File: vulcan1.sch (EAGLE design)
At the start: 0 parts

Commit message: update
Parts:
- added C1, C2, C3: .1u, adafruit:C-US025-040X050
- added C4: 4.7u, adafruit:CPOL-USE5-8.5
- added C5: 10n, adafruit:C-US025-040X050
- added U$1: STM32F103XX-48PIN, vulcan-1:STM32F103XX-48PIN
- added U$2: A2200-A, vulcan-1:A2200-A
- added U$3, U$4: TPS63060, vulcan-1:TPS63060
- added U$5, U$6: ASPI-0520LR, vulcan-1:ASPI-0520LR
- added U$7: AD8494ARMZ, vulcan-1:AD8494ARMZ
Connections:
- new net GND: C4.-, C5.2, U$1.VDDA, U$1.VSS_1, U$1.VSS_2, U$1.VSS_3
- new net N$1: C4.+, U$1.VDD_1, U$1.VDD_2, U$1.VDD_3
- new net N$2: C5.1, U$1.VSSA
- new net N$3: U$4.L1, U$5.P$1
- new net N$4: U$4.L2, U$5.P$2
- new net N$5: U$3.L1, U$6.P$1
- new net N$6: U$3.L2, U$6.P$2

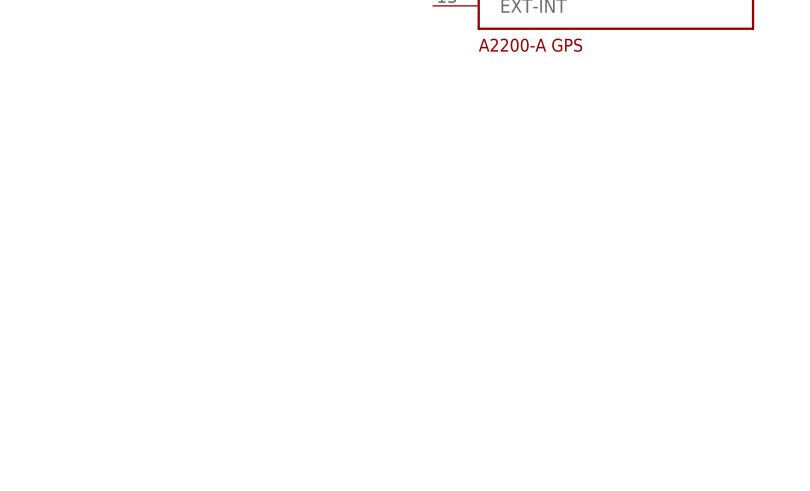
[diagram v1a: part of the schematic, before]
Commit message: update
crystal and RTC
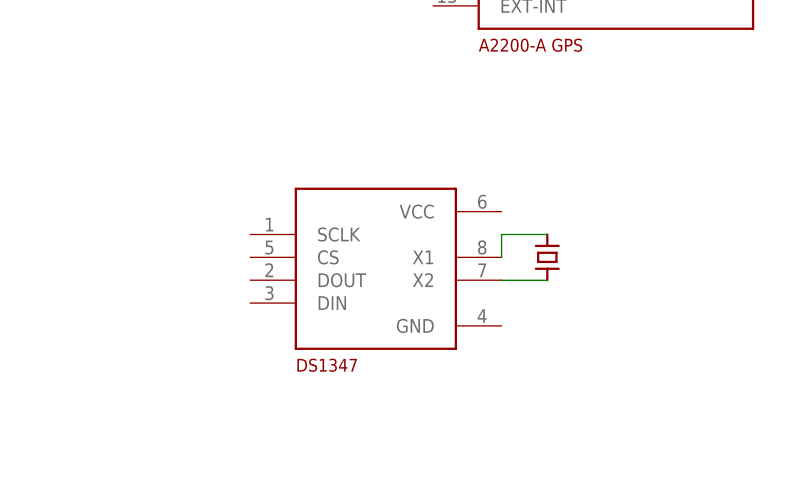
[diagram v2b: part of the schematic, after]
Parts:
- added U$8: 32.768khz, vulcan-1:ECX-306X
- added U$9: DS1347, vulcan-1:DS1347
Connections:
- new net N$7: U$8.P$1, U$9.X2
- new net N$8: U$8.P$2, U$9.X1
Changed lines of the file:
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@@
 <part name="U$6" library="vulcan-1" deviceset="ASPI-0520LR" device=""/>
 <part name="U$7" library="vulcan-1" deviceset="AD8494ARMZ" device=""/>
+<part name="U$8" library="vulcan-1" deviceset="ECX-306X" device="" value="32.768khz"/>
+<part name="U$9" library="vulcan-1" deviceset="DS1347" device=""/>
 </parts>
 <sheets>
@@
 <instance part="U$6" gate="G$1" x="-127" y="109.22"/>
 <instance part="U$7" gate="G$1" x="-7.62" y="101.6"/>
+<instance part="U$8" gate="G$1" x="124.46" y="-25.4" rot="R90"/>
+<instance part="U$9" gate="G$1" x="104.14" y="-30.48"/>
 </instances>
 <busses>
@@
 </segment>
 </net>
+<net name="N$7" class="0">
+<segment>
+<pinref part="U$8" gate="G$1" pin="P$1"/>
+<pinref part="U$9" gate="G$1" pin="X2"/>
+<wire x1="124.46" y1="-27.94" x2="119.38" y2="-27.94" width="0.1524" layer="91"/>
+</segment>
+</net>
+<net name="N$8" class="0">
+<segment>
+<pinref part="U$8" gate="G$1" pin="P$2"/>
+<wire x1="124.46" y1="-22.86" x2="119.38" y2="-22.86" width="0.1524" layer="91"/>
+<pinref part="U$9" gate="G$1" pin="X1"/>
+<wire x1="119.38" y1="-22.86" x2="119.38" y2="-25.4" width="0.1524" layer="91"/>
+</segment>
+</net>

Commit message: update
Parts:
- added BKP-BATT: (no value), adafruit:CR1220THM
- added C10, C9: 18pf, adafruit:C-US025_050-045X075
- added C11, C12, C16, C17, C18, C6, C7: .1u, adafruit:C-US025_050-045X075
- added C13, C8: 10pf, adafruit:C-US025_050-045X075
- added C14, C15: 4700uf, adafruit:CPOL-USE5-13
- added C19: 1u, adafruit:C-US025_050-045X075
- added D1, D2: (no value), adafruit:SCHOTTKY-DIODEDO35-7
- added JP1: M025MM, SparkFun-Connectors:M025MM
- added R1, R3: 560k, adafruit:R-US_0204/7
- added R2, R4: 100k, adafruit:R-US_0204/7
- added R5: 10k, adafruit:R-US_0204/7
- added U$10: HC/49US(AT49), vulcan-1:HC/49US(AT49)
- added U$11: BMP183, vulcan-1:BMP183
- added U$12: XBEE, adafruit:XBEE
- added U1: SD_CARD_SOCKET4UCON, SparkFun-Connectors:SD_CARD_SOCKET4UCON
- C1, C2, C3, C5: device adafruit:C-US025-040X050 -> adafruit:C-US025_050-045X075
- U$8: value 32.768khz -> DS1347; device vulcan-1:ECX-306X -> vulcan-1:DS1347
- U$9: value DS1347 -> ECX-306X; device vulcan-1:DS1347 -> vulcan-1:ECX-306X
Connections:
- new net 3.3A: R1.2, U$3.VOUT
- new net 3.3B: R3.2, U$4.VOUT
- new net CLK: U1.CLK
- new net GPS-DIN: U$2.RX0
- new net GPS-DOUT: U$2.TX0
- new net MISO: U1.DAT0
- new net MOSI: U1.CMD
- new net N$10: C9.1, U$1.PD0_OSC_IN, U$10.P$2
- new net N$11: C7.1, U$3.VAUX
- new net N$12: C18.1, C19.1, D1.C, D2.C, U$8.VCC
- new net N$13: U$11.VDD
- new net N$14: C8.1, R1.1, R2.2, U$3.FB
- new net N$15: C13.1, R3.1, R4.2, U$4.FB
- new net N$16: C16.1, U$2.VCC
- new net N$17: U$2.ANT_GND
- new net N$18: C12.1, U$4.VAUX
- new net N$19: U$2.ANT_IN
- new net N$20: R5.2, U$2.VOUT
- new net N$21: R5.1, U$2.GPIO6
- new net N$22: U$11.VDDIO
- new net N$25: U1.VDD
- new net N$26: D2.A
- new net N$9: C10.1, U$1.PD1_OSC_OUT, U$10.P$1
- new net SD-CS: U1.CD/DAT3
- new net V-BKP: BKP-BATT.+, D1.A
- new net VB-EN: U$4.EN
- new net VBAT: C11.1, C14.+, C15.+, C6.1, JP1.2, U$3.EN, U$3.VIN, U$4.VIN
- new net VCC: C17.1, U$12.VCC
- new net XBEE-CS: U$12.CTS/DIO7
- new net XBEE-DIN: U$12.DIN
- new net XBEE-DOUT: U$12.DOUT
- new net XBEE-RTS: U$12.RTS/AD6/DIO6
- net GND: now also BKP-BATT.-, C1.2, C10.2, C11.2, C12.2, C13.2, C15.-, C16.2, C17.2, C18.2, C19.2, C2.2, C3.2, C6.2, C7.2, C8.2, C9.2, JP1.1, R2.1, R4.1, U$11.GND, U$12.GND, U$2.GND_1, U$2.GND_2, U$3.GND, U$3.PG, U$3.PGND, U$3.PS/SYNC, U$4.GND, U$4.PG, U$4.PGND, U$4.PS/SYNC, U$7.V-, U$8.GND
- net N$1: now also C1.1, C2.1, C3.1
- net N$7: now also U$8.X2, U$9.P$1; no longer U$8.P$1, U$9.X2
- net N$8: now also U$8.X1, U$9.P$2; no longer U$8.P$2, U$9.X1
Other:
- note added: "3.3V supply A"
- note added: "3.3V supply B"
- note added: "7.4V Li-Po and capcitor bank"
- note added: "Backup battery"
- note added: "GPS module"
- note added: "MICROCONTROLLER"
- note added: "PERIPHERALS"
- note added: "POWER"
- note added: "Pressure sensor"
- note added: "Real Time Clock"
- note added: "SD Card"
- note added: "Thermocouple amp"
- note added: "XBEE Radio Module"
- moved on the sheet: C1, C2, C3, C4, C5

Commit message: update
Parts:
- added C20, C21, C22: .1u, adafruit:C-US025-030X050
- added U$13: 2X24HEADER, vulcan-1:2X24HEADER
- C1, C10, C11, C12, C13, C16, C17, C18, C2, C3, C5, C6, C7, C8, C9: device adafruit:C-US025_050-045X075 -> adafruit:C-US025-030X050
- C19: device adafruit:C-US025_050-045X075 -> adafruit:CPOL-USE2,5-6E
- C4: device adafruit:CPOL-USE5-8.5 -> adafruit:CPOL-USE2,5-6E
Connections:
- net N$19 renamed GPS-ANT
- net XBEE-DIN renamed USART3-TX
- removed net CLK: U1.CLK
- removed net GPS-DIN: U$2.RX0
- removed net GPS-DOUT: U$2.TX0
- removed net MISO: U1.DAT0
- removed net MOSI: U1.CMD
- removed net N$1: C1.1, C2.1, C3.1, C4.+, U$1.VDD_1, U$1.VDD_2, U$1.VDD_3
- removed net N$13: U$11.VDD
- removed net N$16: C16.1, U$2.VCC
- removed net N$17: U$2.ANT_GND
- removed net N$22: U$11.VDDIO
- removed net N$25: U1.VDD
- removed net N$26: D2.A
- removed net VCC: C17.1, U$12.VCC
- removed net XBEE-CS: U$12.CTS/DIO7
- removed net XBEE-DOUT: U$12.DOUT
- removed net XBEE-RTS: U$12.RTS/AD6/DIO6
- new net ACC-CS: U$13.P$6
- new net ACC-FLAG: U$13.P$7
- new net ACC-RST: U$13.P$8
- new net BOOT0: U$1.BOOT0
- new net BOOT1: U$1.PB2
- new net N$23: U$2.ON_OFF
- new net N$24: U$7.+IN, U$7.-IN
- new net N$30: U$7.OUT, U$7.SENSE
- new net PS-CS: U$11.CSB
- new net RTC-CS: U$8.CS
- new net SPI-MISO: U$1.PA6, U$11.SDO, U$13.P$4, U$8.DOUT, U1.DAT0
- new net SPI-MOSI: U$1.PA7, U$11.SDI, U$13.P$5, U$8.DIN, U1.CMD
- new net SPI-NSS: U$1.PA4
- new net SPI-SCK: U$1.PA5, U$11.SCK, U$13.P$3, U$8.SCLK, U1.CLK
- new net USART1-RX: U$1.PA10
- new net USART1-TX: U$1.PA9
- new net USART2-RX: U$1.PA3, U$2.TX0
- new net USART2-TX: U$1.PA2, U$1.PB10, U$2.RX0
- new net USART3-CTS: U$1.PB13, U$12.CTS/DIO7
- new net USART3-RTS: U$1.PB14, U$12.RTS/AD6/DIO6
- new net USART3-RX: U$1.PB11, U$12.DOUT
- net 3.3A: now also C1.1, C2.1, C20.1, C21.1, C22.1, C3.1, C4.+, D2.A, U$1.VDD_1, U$1.VDD_2, U$1.VDD_3, U$11.VDD, U$11.VDDIO, U$13.P$10, U$13.P$11, U$13.P$12, U$7.V+, U1.VDD
- net 3.3B: now also C16.1, C17.1, U$12.VCC, U$2.VCC
- net GND: now also C19.-, C20.2, C21.2, C22.2, U$13.P$13, U$13.P$14, U$13.P$15, U$2.ANT_GND, U$7.REF, U1.VSS1, U1.VSS2; no longer C19.2
- net N$12: now also C19.+; no longer C19.1
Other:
- note added: "Accelerometer mount"

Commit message: update-all but RF traces and gnd plane done
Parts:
- removed U$13: 2X24HEADER, vulcan-1:2X24HEADER
- added A2200-A: A2200-A, vulcan-1:A2200-A
- added FUSE: FUSE, adafruit:R-US_0204/7
- added JP2: (no value), adafruit:PINHD-1X8CLEANBIG
- added JP3: (no value), adafruit:PINHD-1X3CB
- added Q1, Q2: IRF540, transistor-power:IRF540
- added R6, R7: 10k, adafruit:R-US_0204/7
- added T1, T2: 2N3904, transistor:2N3904
- added TPS63060-A, TPS63060-B: TPS63060, vulcan-1:TPS63060
- C14: value 4700uf -> .1u; device adafruit:CPOL-USE5-13 -> adafruit:C-US025-030X050
- U$2: value A2200-A -> 2X3; device vulcan-1:A2200-A -> vulcan-1:2X3
- U$3, U$4: value TPS63060 -> 1X2BIG; device vulcan-1:TPS63060 -> vulcan-1:1X2BIG
- U$7: value AD8494ARMZ -> SMA; device vulcan-1:AD8494ARMZ -> vulcan-1:SMA
- renumbered U$11 to BMP183, U$12 to XBEE, U$8 to DS1347, U1 to SD
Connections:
- removed net N$23: U$2.ON_OFF
- removed net N$24: U$7.+IN, U$7.-IN
- removed net N$30: U$7.OUT, U$7.SENSE
- removed net SPI-NSS: U$1.PA4
- removed net VB-EN: U$4.EN
- new net EMATCH1: T1.B
- new net EMATCH2: T2.B
- new net GPS-CS: A2200-A.ON_OFF, U$1.PA1
- new net N$1: Q1.G, R6.1, T1.C
- new net N$13: Q1.D, U$3.2
- new net N$16: Q2.G, R7.1, T2.C
- new net N$17: Q2.D, U$4.2
- new net VB-CS: TPS63060-B.EN, U$1.PB8
- new net VBAT-F: FUSE.2, R6.2, R7.2, U$3.1, U$4.1
- net 3.3A: now also C14.1, JP2.8, TPS63060-A.VOUT, U$2.1, U$2.2; no longer C22.1, U$13.P$10, U$13.P$11, U$13.P$12, U$3.VOUT, U$7.V+
- net 3.3B: now also A2200-A.VCC, C22.1, TPS63060-B.VOUT; no longer U$2.VCC, U$4.VOUT
- net ACC-CS: now also JP2.5, U$1.PA8; no longer U$13.P$6
- net ACC-FLAG: now also JP2.6; no longer U$13.P$7
- net ACC-RST: now also JP2.4; no longer U$13.P$8
- net BOOT0: now also U$2.3
- net BOOT1: now also U$2.4
- net GND: now also A2200-A.ANT_GND, A2200-A.GND_1, A2200-A.GND_2, C14.2, JP2.7, JP3.3, Q1.S, Q2.S, T1.E, T2.E, TPS63060-A.GND, TPS63060-A.PG, TPS63060-A.PGND, TPS63060-A.PS/SYNC, TPS63060-B.GND, TPS63060-B.PG, TPS63060-B.PGND, TPS63060-B.PS/SYNC, U$2.5, U$2.6; no longer U$13.P$13, U$13.P$14, U$13.P$15, U$2.ANT_GND, U$2.GND_1, U$2.GND_2, U$3.GND, U$3.PG, U$3.PGND, U$3.PS/SYNC, U$4.GND, U$4.PG, U$4.PGND, U$4.PS/SYNC, U$7.REF, U$7.V-
- net GPS-ANT: now also A2200-A.ANT_IN, U$7.IN; no longer U$2.ANT_IN
- net N$11: now also TPS63060-A.VAUX; no longer U$3.VAUX
- net N$14: now also TPS63060-A.FB; no longer U$3.FB
- net N$15: now also TPS63060-B.FB; no longer U$4.FB
- net N$18: now also TPS63060-B.VAUX; no longer U$4.VAUX
- net N$20: now also A2200-A.VOUT; no longer U$2.VOUT
- net N$21: now also A2200-A.GPIO6; no longer U$2.GPIO6
- net N$3: now also TPS63060-B.L1; no longer U$4.L1
- net N$4: now also TPS63060-B.L2; no longer U$4.L2
- net N$5: now also TPS63060-A.L1; no longer U$3.L1
- net N$6: now also TPS63060-A.L2; no longer U$3.L2
- net PS-CS: now also U$1.PA4
- net RTC-CS: now also U$1.PB12
- net SD-CS: now also U$1.PB15
- net SPI-MISO: now also JP2.2; no longer U$13.P$4
- net SPI-MOSI: now also JP2.1; no longer U$13.P$5
- net SPI-SCK: now also JP2.3; no longer U$13.P$3
- net USART1-RX: now also JP3.2
- net USART1-TX: now also JP3.1
- net USART2-RX: now also A2200-A.TX0; no longer U$2.TX0
- net USART2-TX: now also A2200-A.RX0; no longer U$1.PB10, U$2.RX0
- net USART3-TX: now also U$1.PB10
- net VBAT: now also FUSE.1, TPS63060-A.EN, TPS63060-A.VIN, TPS63060-B.VIN; no longer C14.+, U$3.EN, U$3.VIN, U$4.VIN
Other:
- note added: "Accelerometer Header"
- note added: "BOOT header"
- note added: "E-Matches"
- note removed: "Accelerometer mount"
- note removed: "Thermocouple amp"
- moved on the sheet: C1, C10, C2, C20, C22, C3, C4, C5, C9

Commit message: update-gnd done
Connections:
- net GND: now also U$7.OUT
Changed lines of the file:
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@@
 <pinref part="GND17" gate="1" pin="GND"/>
 <wire x1="139.7" y1="7.62" x2="149.86" y2="7.62" width="0.1524" layer="91"/>
-<wire x1="149.86" y1="7.62" x2="149.86" y2="2.54" width="0.1524" layer="91"/>
+<wire x1="149.86" y1="7.62" x2="149.86" y2="5.08" width="0.1524" layer="91"/>
+<pinref part="U$7" gate="G$1" pin="OUT"/>
+<wire x1="149.86" y1="5.08" x2="149.86" y2="2.54" width="0.1524" layer="91"/>
+<junction x="149.86" y="5.08"/>
 </segment>
 <segment>

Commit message: labels cleaned up
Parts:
- removed U$10: HC/49US(AT49), vulcan-1:HC/49US(AT49)
- added U$8: 1X2BIG, vulcan-1:1X2BIG
- C10: value 18pf -> .1u
- C12: value .1u -> 1u; device adafruit:C-US025-030X050 -> adafruit:CPOL-USE2,5-6E
- C13, C8: value 10pf -> .1u
- C15: value 4700uf -> .1u; device adafruit:CPOL-USE5-13 -> adafruit:C-US025-030X050
- C16: value .1u -> 4700uf; device adafruit:C-US025-030X050 -> adafruit:CPOL-USE5-13
- C19: value 1u -> .1u; device adafruit:CPOL-USE2,5-6E -> adafruit:C-US025-030X050
- C20, C22: value .1u -> 10pf
- C3: value .1u -> 18pf
- C4: value 4.7u -> 18pf; device adafruit:CPOL-USE2,5-6E -> adafruit:C-US025-030X050
- C9: value 18pf -> 4.7u; device adafruit:C-US025-030X050 -> adafruit:CPOL-USE2,5-6E
- JP1: value M025MM -> (none); device SparkFun-Connectors:M025MM -> adafruit:PINHD-1X8CLEANBIG
- JP2: value (none) -> M025MM; device adafruit:PINHD-1X8CLEANBIG -> SparkFun-Connectors:M025MM
- R1: value 560k -> 10k
- R2, R4: value 100k -> 560k
- R3: value 560k -> 100k
- R5: value 10k -> 100k
- U$1: value STM32F103XX-48PIN -> SMA; device vulcan-1:STM32F103XX-48PIN -> vulcan-1:SMA
- U$2: value 2X3 -> HC/49US(AT49); device vulcan-1:2X3 -> vulcan-1:HC/49US(AT49)
- U$3: value 1X2BIG -> STM32F103XX-48PIN; device vulcan-1:1X2BIG -> vulcan-1:STM32F103XX-48PIN
- U$4: value 1X2BIG -> ECX-306X; device vulcan-1:1X2BIG -> vulcan-1:ECX-306X
- U$7: value SMA -> 2X3; device vulcan-1:SMA -> vulcan-1:2X3
- U$9: value ECX-306X -> 1X2BIG; device vulcan-1:ECX-306X -> vulcan-1:1X2BIG
- renumbered BMP183 to BMP1, DS1347 to DS1
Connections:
- net 3.3A: now also C10.1, C11.1, C6.1, C7.1, C8.1, C9.+, JP1.8, R2.2, U$3.VDD_1, U$3.VDD_2, U$3.VDD_3, U$7.1, U$7.2; no longer C1.1, C2.1, C20.1, C21.1, C3.1, C4.+, JP2.8, R1.2, U$1.VDD_1, U$1.VDD_2, U$1.VDD_3, U$2.1, U$2.2
- net 3.3B: now also C1.1, C15.1, C2.1, R4.2; no longer C16.1, C17.1, C22.1, R3.2
- net ACC-CS: now also JP1.5, U$3.PA8; no longer JP2.5, U$1.PA8
- net ACC-FLAG: now also JP1.6; no longer JP2.6
- net ACC-RST: now also JP1.4; no longer JP2.4
- net BOOT0: now also U$3.BOOT0, U$7.3; no longer U$1.BOOT0, U$2.3
- net BOOT1: now also U$3.PB2, U$7.4; no longer U$1.PB2, U$2.4
- net EMATCH1: now also T2.B; no longer T1.B
- net EMATCH2: now also T1.B; no longer T2.B
- net GND: now also C12.-, C15.2, C16.-, C19.2, C4.2, C9.-, JP1.7, JP2.1, R3.1, R5.1, U$1.OUT, U$3.VDDA, U$3.VSS_1, U$3.VSS_2, U$3.VSS_3, U$7.5, U$7.6; no longer C12.2, C15.-, C16.2, C19.-, C4.-, C9.2, JP1.1, JP2.7, R2.1, R4.1, U$1.VDDA, U$1.VSS_1, U$1.VSS_2, U$1.VSS_3, U$2.5, U$2.6, U$7.OUT
- net GPS-ANT: now also U$1.IN; no longer U$7.IN
- net GPS-CS: now also U$3.PA1; no longer U$1.PA1
- net N$10: now also C4.1, U$2.P$2, U$3.PD0_OSC_IN; no longer C9.1, U$1.PD0_OSC_IN, U$10.P$2
- net N$11: now also C19.1; no longer C7.1
- net N$12: now also C12.+, C13.1; no longer C18.1, C19.+
- net N$13: now also Q2.D, U$9.2; no longer Q1.D, U$3.2
- net N$14: now also C20.1, R2.1, R3.2; no longer C8.1, R1.1, R2.2
- net N$15: now also C22.1, R4.1, R5.2; no longer C13.1, R3.1, R4.2
- net N$17: now also Q1.D, U$8.2; no longer Q2.D, U$4.2
- net N$18: now also C21.1; no longer C12.1
- net N$2: now also U$3.VSSA; no longer U$1.VSSA
- net N$20: now also R1.2; no longer R5.2
- net N$21: now also R1.1; no longer R5.1
- net N$3: now also U$6.P$1; no longer U$5.P$1
- net N$4: now also U$6.P$2; no longer U$5.P$2
- net N$5: now also U$5.P$1; no longer U$6.P$1
- net N$6: now also U$5.P$2; no longer U$6.P$2
- net N$7: now also U$4.P$1; no longer U$9.P$1
- net N$8: now also U$4.P$2; no longer U$9.P$2
- net N$9: now also C3.1, U$2.P$1, U$3.PD1_OSC_OUT; no longer C10.1, U$1.PD1_OSC_OUT, U$10.P$1
- net PS-CS: now also U$3.PA4; no longer U$1.PA4
- net RTC-CS: now also U$3.PB12; no longer U$1.PB12
- net SD-CS: now also U$3.PB15; no longer U$1.PB15
- net SPI-MISO: now also JP1.2, U$3.PA6; no longer JP2.2, U$1.PA6
- net SPI-MOSI: now also JP1.1, U$3.PA7; no longer JP2.1, U$1.PA7
- net SPI-SCK: now also JP1.3, U$3.PA5; no longer JP2.3, U$1.PA5
- net USART1-RX: now also U$3.PA10; no longer U$1.PA10
- net USART1-TX: now also U$3.PA9; no longer U$1.PA9
- net USART2-RX: now also U$3.PA3; no longer U$1.PA3
- net USART2-TX: now also U$3.PA2; no longer U$1.PA2
- net USART3-CTS: now also U$3.PB13; no longer U$1.PB13
- net USART3-RTS: now also U$3.PB14; no longer U$1.PB14
- net USART3-RX: now also U$3.PB11; no longer U$1.PB11
- net USART3-TX: now also U$3.PB10; no longer U$1.PB10
- net VB-CS: now also U$3.PB8; no longer U$1.PB8
- net VBAT: now also C16.+, C17.1, C18.1, JP2.2; no longer C11.1, C15.+, C6.1, JP1.2
- net VBAT-F: now also U$8.1, U$9.1; no longer U$3.1, U$4.1
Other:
- moved on the sheet: C1, C10, C11, C13, C17, C18, C2, C20, C21, C22, C3, C6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

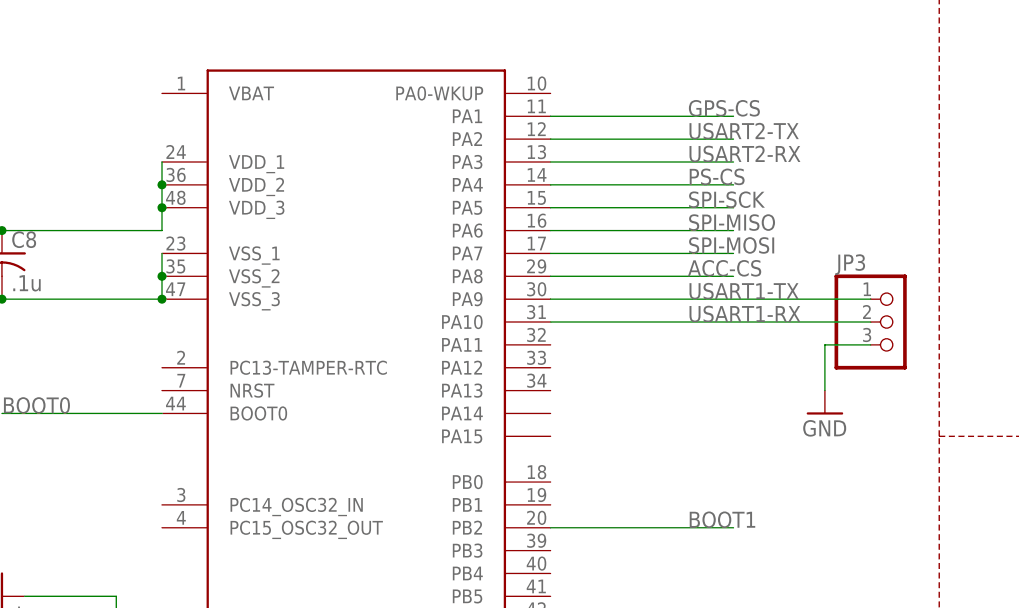
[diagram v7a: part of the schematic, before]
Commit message: accelerometer reset and flag pins added
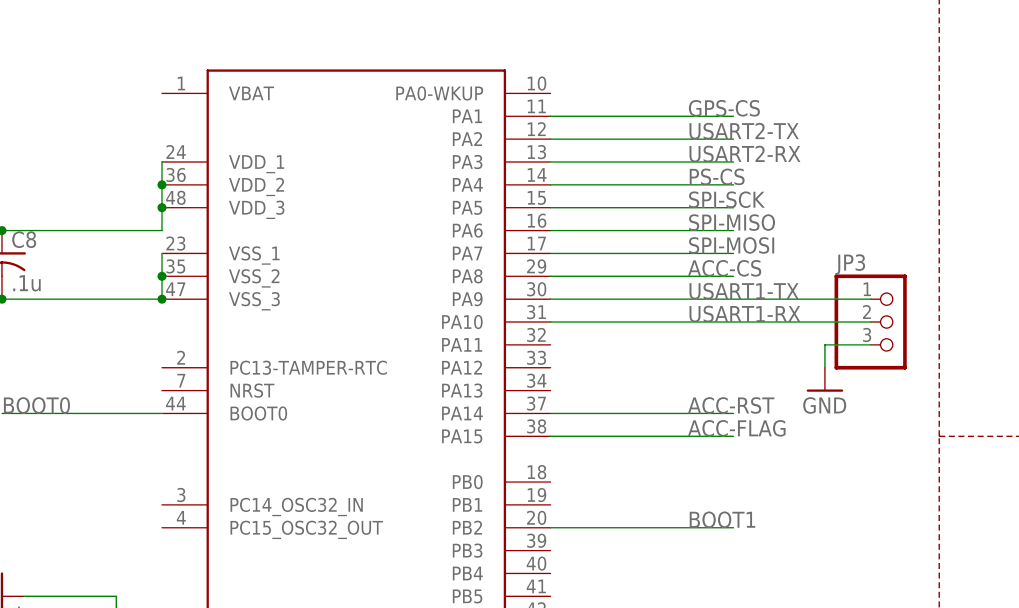
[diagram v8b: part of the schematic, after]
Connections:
- net ACC-FLAG: now also U$3.PA15
- net ACC-RST: now also U$3.PA14
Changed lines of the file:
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@@
 <instance part="C15" gate="G$1" x="-93.98" y="30.48"/>
 <instance part="JP3" gate="A" x="60.96" y="40.64"/>
-<instance part="GND20" gate="1" x="53.34" y="30.48"/>
+<instance part="GND20" gate="1" x="53.34" y="33.02"/>
 <instance part="U$1" gate="G$1" x="144.78" y="5.08"/>
 </instances>
@@
 <wire x1="-45.72" y1="43.18" x2="-38.1" y2="43.18" width="0.1524" layer="91"/>
 <wire x1="-38.1" y1="43.18" x2="-20.32" y2="43.18" width="0.1524" layer="91"/>
-<wire x1="-20.32" y1="43.18" x2="-20.32" y2="45.72" width="0.1524" layer="91"/>
 <junction x="-20.32" y="43.18"/>
 <pinref part="U$3" gate="G$1" pin="VSS_1"/>
-<wire x1="-20.32" y1="45.72" x2="-20.32" y2="48.26" width="0.1524" layer="91"/>
 <junction x="-20.32" y="45.72"/>
 <pinref part="C8" gate="G$1" pin="2"/>
@@
 <pinref part="C10" gate="G$1" pin="2"/>
 <junction x="-53.34" y="43.18"/>
+<wire x1="-20.32" y1="45.72" x2="-20.32" y2="48.26" width="0.1524" layer="91"/>
+<wire x1="-20.32" y1="43.18" x2="-20.32" y2="45.72" width="0.1524" layer="91"/>
 </segment>
 <segment>
@@
 <pinref part="JP3" gate="A" pin="3"/>
 <wire x1="58.42" y1="38.1" x2="53.34" y2="38.1" width="0.1524" layer="91"/>
-<wire x1="53.34" y1="38.1" x2="53.34" y2="33.02" width="0.1524" layer="91"/>
+<wire x1="53.34" y1="38.1" x2="53.34" y2="35.56" width="0.1524" layer="91"/>
 <pinref part="GND20" gate="1" pin="GND"/>
 </segment>
@@
 <pinref part="U$3" gate="G$1" pin="VDD_3"/>
 <pinref part="U$3" gate="G$1" pin="VDD_2"/>
-<wire x1="-20.32" y1="53.34" x2="-20.32" y2="55.88" width="0.1524" layer="91"/>
 <pinref part="U$3" gate="G$1" pin="VDD_1"/>
-<wire x1="-20.32" y1="58.42" x2="-20.32" y2="55.88" width="0.1524" layer="91"/>
 <junction x="-20.32" y="55.88"/>
 <wire x1="-20.32" y1="53.34" x2="-20.32" y2="50.8" width="0.1524" layer="91"/>
@@
 <junction x="-53.34" y="50.8"/>
 <label x="-60.96" y="50.8" size="1.778" layer="95"/>
+<wire x1="-20.32" y1="53.34" x2="-20.32" y2="55.88" width="0.1524" layer="91"/>
+<wire x1="-20.32" y1="55.88" x2="-20.32" y2="58.42" width="0.1524" layer="91"/>
 </segment>
 <segment>
@@
 <pinref part="JP1" gate="G$1" pin="6"/>
 </segment>
+<segment>
+<pinref part="U$3" gate="G$1" pin="PA15"/>
+<wire x1="22.86" y1="27.94" x2="43.18" y2="27.94" width="0.1524" layer="91"/>
+<label x="38.1" y="27.94" size="1.778" layer="95"/>
+</segment>
 </net>
 <net name="RTC-CS" class="0">
@@
 <label x="177.8" y="68.58" size="1.778" layer="95"/>
 </segment>
-</net>
+<segment>
+<pinref part="U$3" gate="G$1" pin="PA14"/>
+<wire x1="22.86" y1="30.48" x2="43.18" y2="30.48" width="0.1524" layer="91"/>
+<label x="38.1" y="30.48" size="1.778" layer="95"/>
+</segment>
+</net>
